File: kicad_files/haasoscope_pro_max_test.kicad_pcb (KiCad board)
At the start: 10 copper layers, 200 x 125 mm, 8 parts, among them IC1 ADC12DL500ACF_Aligned, U1 MT53D512M16D1DS_Aligned, U2 FT601Q_Aligned, U3 Ti90G529_Functions

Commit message: test_fanout_and_route.py from scratch
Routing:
- net Net-(U2A-DATA_11): track 8.84 -> 0.00 mm, vias 1 -> 0
- net Net-(U2A-DATA_14): track 8.73 -> 0.00 mm, vias 1 -> 0
- net Net-(U2A-DATA_17): track 8.20 -> 0.00 mm, vias 1 -> 0
- net Net-(U2A-DATA_20): track 8.20 -> 0.00 mm, vias 1 -> 0
- net Net-(U2A-DATA_0): track 7.93 -> 0.00 mm, vias 1 -> 0
- net Net-(U2A-DATA_16): track 6.87 -> 0.00 mm, vias 1 -> 0
- net Net-(U2A-DATA_2): track 6.70 -> 0.00 mm
- net Net-(U2A-DATA_23): track 6.60 -> 0.00 mm, vias 1 -> 0
- net Net-(U2A-DATA_22): track 6.07 -> 0.00 mm, vias 1 -> 0
- net Net-(U2A-DATA_5): track 5.90 -> 0.00 mm, vias 1 -> 0
- net Net-(U2A-DATA_9): track 5.80 -> 0.00 mm, vias 1 -> 0
- net Net-(U2A-DATA_24): track 5.64 -> 0.00 mm, vias 1 -> 0
- net Net-(U2A-DATA_8): track 5.53 -> 0.00 mm, vias 1 -> 0
- net Net-(U2A-DATA_18): track 5.53 -> 0.00 mm, vias 1 -> 0
- net Net-(U2A-DATA_13): track 5.37 -> 0.00 mm, vias 1 -> 0
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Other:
- board size 200 x 125 mm -> 110.6 x 48.6 mm

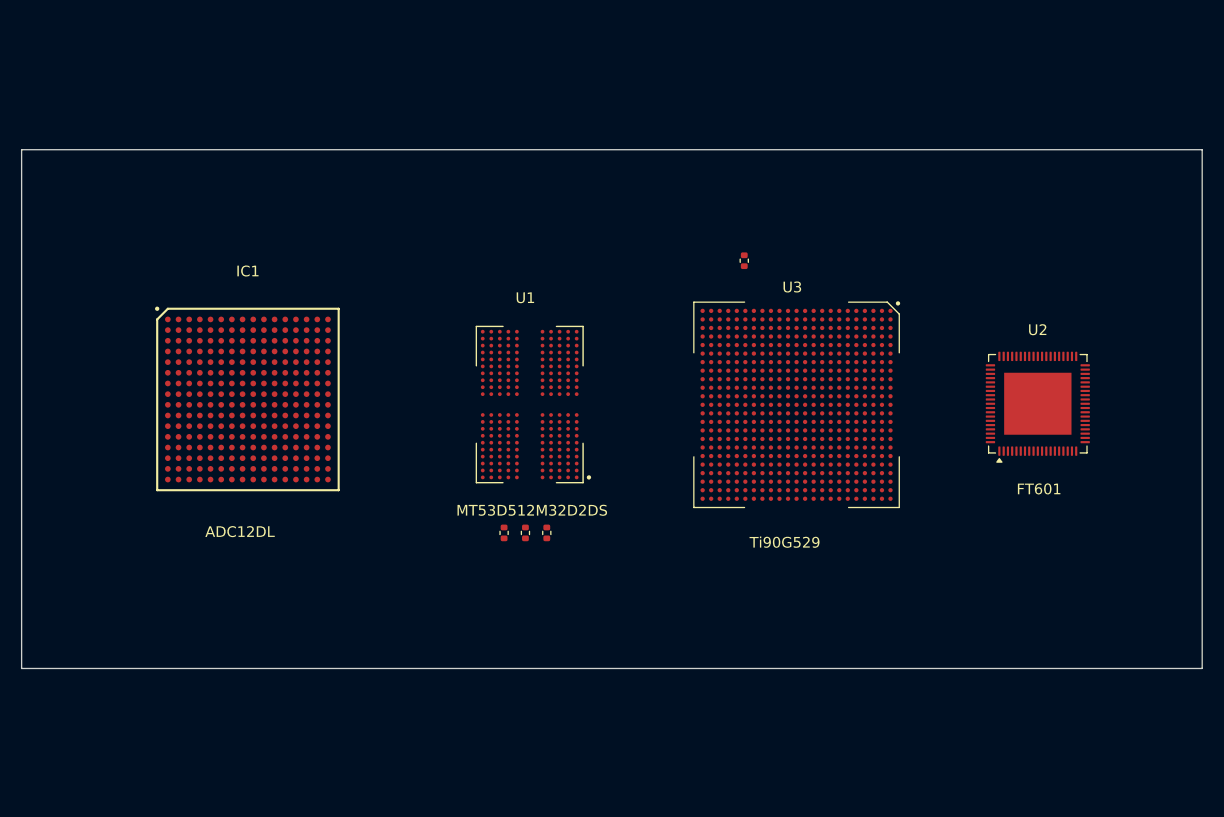
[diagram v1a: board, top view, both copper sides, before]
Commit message: --no-inner-top-layer for bga fanout
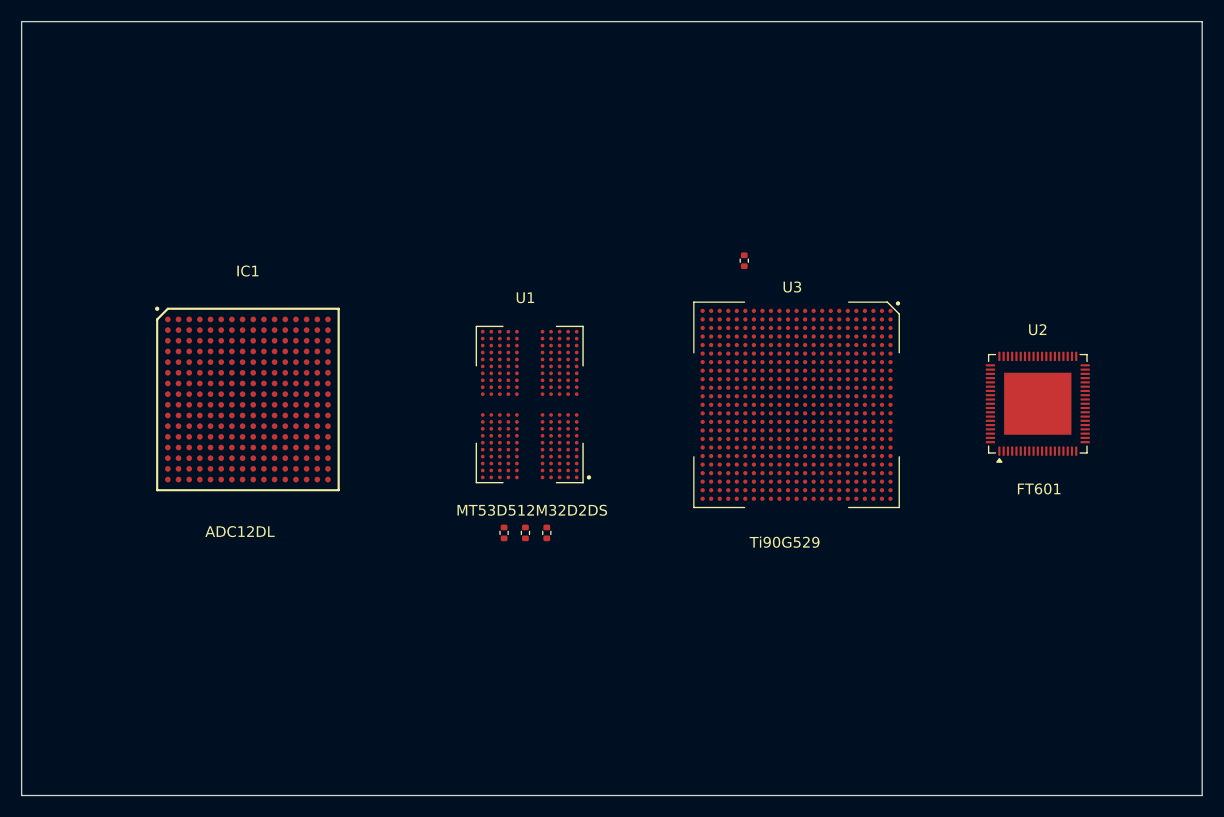
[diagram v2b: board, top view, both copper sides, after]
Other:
- board size 110.6 x 48.6 mm -> 110.6 x 72.5 mm
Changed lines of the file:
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@@
 	)
 	(gr_rect
-		(start 122.8 79.1)
-		(end 233.4 127.7)
+		(start 122.8 67.1)
+		(end 233.4 139.6)
 		(stroke
 			(width 0.05)

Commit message: add gnd plane
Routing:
- added copper zone on F.Cu, net GND
- added copper zone on In5.Cu, net GND
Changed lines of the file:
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@@
+		)
+	)
+	(zone
+		(net 690)
+		(net_name "GND")
+		(layers "F.Cu" "In5.Cu")
+		(hatch edge 0.5)
+		(connect_pads
+			(clearance 0.1)
+		)
+		(min_thickness 0.1)
+		(filled_areas_thickness no)
+		(fill yes
+			(thermal_gap 0.2)
+			(thermal_bridge_width 0.2)
+		)
+		(polygon
+			(pts
+				(xy 123.3 67.5) (xy 123.4 139) (xy 233 139.1) (xy 233.1 67.5)
+			)
 		)
 	)

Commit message: add gnd plane
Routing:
- removed copper zone on F.Cu, net GND
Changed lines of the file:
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@@
 		(net 690)
 		(net_name "GND")
-		(layers "F.Cu" "In5.Cu")
+		(layer "In5.Cu")
 		(hatch edge 0.5)
 		(connect_pads

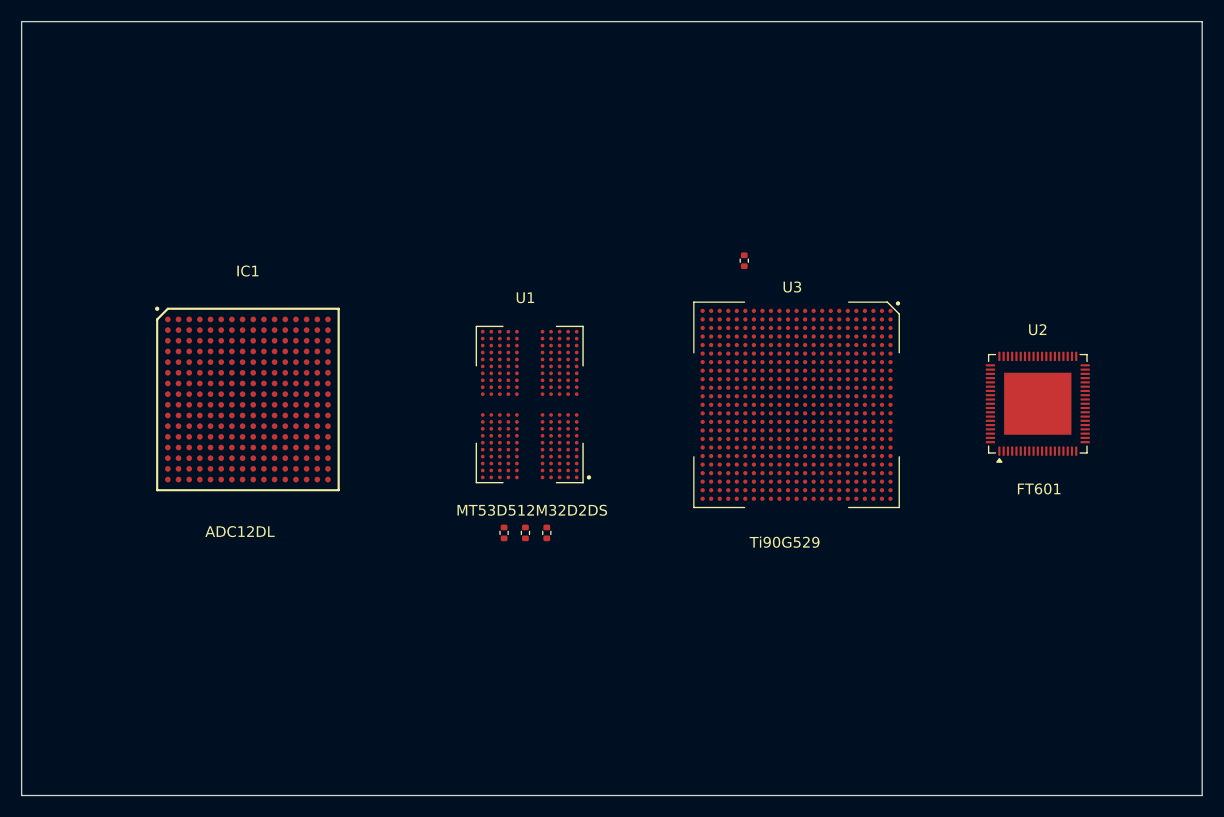
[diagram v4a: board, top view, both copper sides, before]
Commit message: HSPro max gnd and power test
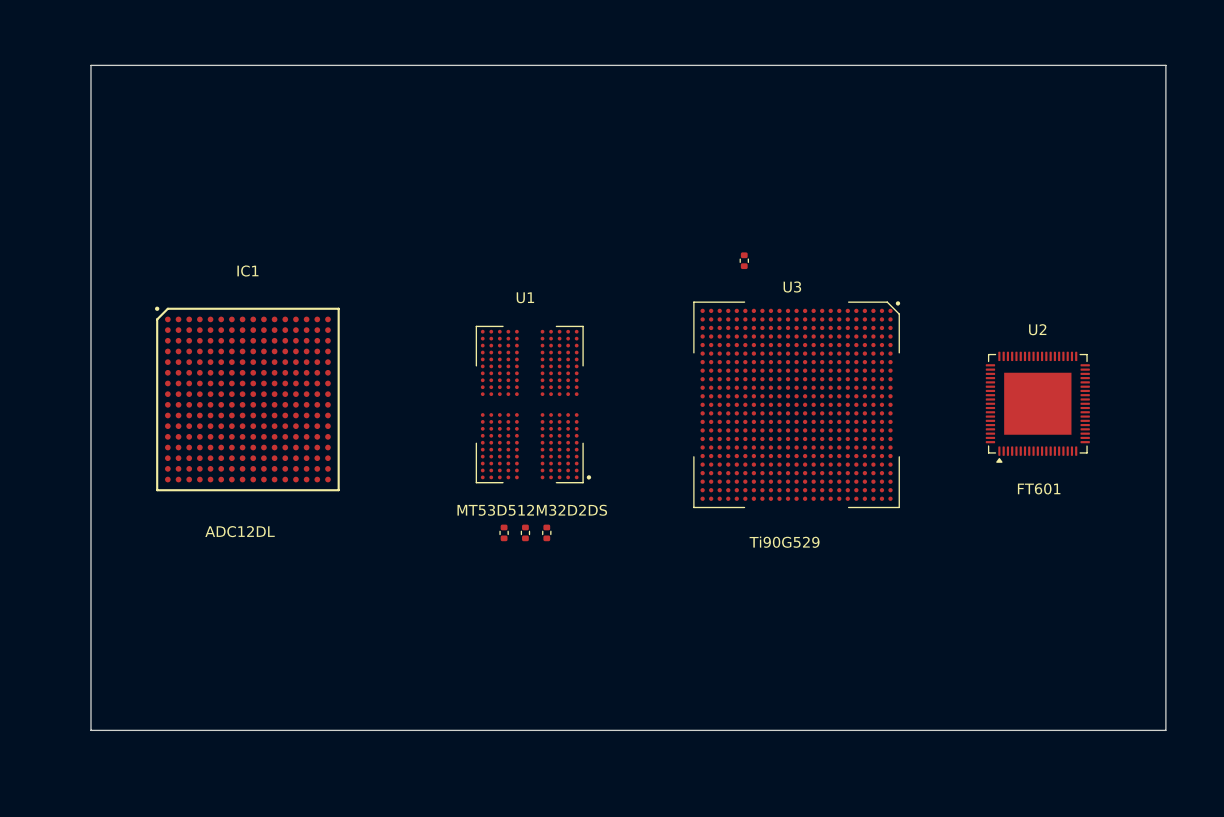
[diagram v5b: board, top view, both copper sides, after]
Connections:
- IC1 pad A1: unconnected-(IC1F-AGND_1-PadA1) -> GND
- IC1 pad A15: unconnected-(IC1F-DGND_1-PadA15) -> GND
- IC1 pad A16: unconnected-(IC1F-DGND_2-PadA16) -> GND
- IC1 pad A2: unconnected-(IC1F-AGND_2-PadA2) -> GND
- IC1 pad A3: unconnected-(IC1F-AGND_3-PadA3) -> GND
- IC1 pad A6: unconnected-(IC1F-AGND_4-PadA6) -> GND
- IC1 pad A7: unconnected-(IC1F-AGND_5-PadA7) -> GND
- IC1 pad B3: unconnected-(IC1F-AGND_6-PadB3) -> GND
- IC1 pad B4: unconnected-(IC1F-AGND_7-PadB4) -> GND
- IC1 pad B5: unconnected-(IC1F-AGND_8-PadB5) -> GND
- IC1 pad B6: unconnected-(IC1F-AGND_9-PadB6) -> GND
- IC1 pad B7: unconnected-(IC1F-AGND_10-PadB7) -> GND
- IC1 pad C1: unconnected-(IC1F-AGND_11-PadC1) -> GND
- IC1 pad C2: unconnected-(IC1F-AGND_12-PadC2) -> GND
- IC1 pad C3: unconnected-(IC1F-AGND_13-PadC3) -> GND
- IC1 pad C4: unconnected-(IC1F-AGND_14-PadC4) -> GND
- IC1 pad C5: unconnected-(IC1F-AGND_15-PadC5) -> GND
- IC1 pad C6: unconnected-(IC1F-AGND_16-PadC6) -> GND
- IC1 pad C7: unconnected-(IC1F-AGND_17-PadC7) -> GND
- IC1 pad D3: unconnected-(IC1F-AGND_18-PadD3) -> GND
- IC1 pad D4: unconnected-(IC1F-AGND_19-PadD4) -> GND
- IC1 pad D5: unconnected-(IC1F-AGND_20-PadD5) -> GND
- IC1 pad D6: unconnected-(IC1F-AGND_21-PadD6) -> GND
- IC1 pad D7: unconnected-(IC1F-DGND_3-PadD7) -> GND
- IC1 pad E3: unconnected-(IC1F-AGND_22-PadE3) -> GND
- IC1 pad E4: unconnected-(IC1F-VA11_1-PadE4) -> /fpga_adc/VA11
- IC1 pad E5: unconnected-(IC1F-VA11_2-PadE5) -> /fpga_adc/VA11
- IC1 pad E6: unconnected-(IC1F-VA11_3-PadE6) -> /fpga_adc/VA11
- IC1 pad E7: unconnected-(IC1F-DGND_4-PadE7) -> GND
- IC1 pad E8: unconnected-(IC1F-VD11_1-PadE8) -> /fpga_adc/VD11
- IC1 pad F1: unconnected-(IC1F-AGND_23-PadF1) -> GND
- IC1 pad F2: unconnected-(IC1F-AGND_24-PadF2) -> GND
- IC1 pad F3: unconnected-(IC1F-VA11_4-PadF3) -> /fpga_adc/VA11
- IC1 pad F4: unconnected-(IC1F-VA11_5-PadF4) -> /fpga_adc/VA11
- IC1 pad F5: unconnected-(IC1F-VA11_6-PadF5) -> /fpga_adc/VA11
- IC1 pad F6: unconnected-(IC1F-VA11_7-PadF6) -> /fpga_adc/VA11
- IC1 pad F7: unconnected-(IC1F-DGND_5-PadF7) -> GND
- IC1 pad F8: unconnected-(IC1F-VD11_2-PadF8) -> /fpga_adc/VD11
- IC1 pad G1: unconnected-(IC1F-AGND_25-PadG1) -> GND
- IC1 pad G11: unconnected-(IC1F-VLVDS_1-PadG11) -> /fpga_adc/VLVDS
- IC1 pad G12: unconnected-(IC1F-VLVDS_2-PadG12) -> /fpga_adc/VLVDS
- IC1 pad G2: unconnected-(IC1F-AGND_26-PadG2) -> GND
- IC1 pad G3: unconnected-(IC1F-VA19_1-PadG3) -> /fpga_adc/VA19
- IC1 pad G4: unconnected-(IC1F-VA19_2-PadG4) -> /fpga_adc/VA19
- IC1 pad G5: unconnected-(IC1F-VA19_3-PadG5) -> /fpga_adc/VA19
- IC1 pad G6: unconnected-(IC1F-VA19_4-PadG6) -> /fpga_adc/VA19
- IC1 pad G7: unconnected-(IC1F-DGND_6-PadG7) -> GND
- IC1 pad G8: unconnected-(IC1F-VD11_3-PadG8) -> /fpga_adc/VD11
- IC1 pad H11: unconnected-(IC1F-VLVDS_3-PadH11) -> /fpga_adc/VLVDS
- IC1 pad H12: unconnected-(IC1F-VLVDS_4-PadH12) -> /fpga_adc/VLVDS
- IC1 pad H13: unconnected-(IC1F-VLVDS_5-PadH13) -> /fpga_adc/VLVDS
- IC1 pad H14: unconnected-(IC1F-DGND_9-PadH14) -> GND
- IC1 pad H2: unconnected-(IC1F-AGND_27-PadH2) -> GND
- IC1 pad H3: unconnected-(IC1F-VA19_5-PadH3) -> /fpga_adc/VA19
- IC1 pad H4: unconnected-(IC1F-VA19_6-PadH4) -> /fpga_adc/VA19
- IC1 pad H5: unconnected-(IC1F-VA19_7-PadH5) -> /fpga_adc/VA19
- IC1 pad H6: unconnected-(IC1F-VA19_8-PadH6) -> /fpga_adc/VA19
- IC1 pad H7: unconnected-(IC1F-DGND_7-PadH7) -> GND
- IC1 pad H8: unconnected-(IC1F-DGND_8-PadH8) -> GND
- IC1 pad J11: unconnected-(IC1F-VLVDS_6-PadJ11) -> /fpga_adc/VLVDS
- IC1 pad J12: unconnected-(IC1F-VLVDS_7-PadJ12) -> /fpga_adc/VLVDS
- IC1 pad J13: unconnected-(IC1F-VLVDS_8-PadJ13) -> /fpga_adc/VLVDS
- IC1 pad J14: unconnected-(IC1F-DGND_12-PadJ14) -> GND
- IC1 pad J2: unconnected-(IC1F-AGND_28-PadJ2) -> GND
- IC1 pad J3: unconnected-(IC1F-VA19_9-PadJ3) -> /fpga_adc/VA19
- IC1 pad J4: unconnected-(IC1F-VA19_10-PadJ4) -> /fpga_adc/VA19
- IC1 pad J5: unconnected-(IC1F-VA19_11-PadJ5) -> /fpga_adc/VA19
- IC1 pad J6: unconnected-(IC1F-VA19_12-PadJ6) -> /fpga_adc/VA19
- IC1 pad J7: unconnected-(IC1F-DGND_10-PadJ7) -> GND
- IC1 pad J8: unconnected-(IC1F-DGND_11-PadJ8) -> GND
- IC1 pad K1: unconnected-(IC1F-AGND_29-PadK1) -> GND
- IC1 pad K11: unconnected-(IC1F-VLVDS_9-PadK11) -> /fpga_adc/VLVDS
- IC1 pad K12: unconnected-(IC1F-VLVDS_10-PadK12) -> /fpga_adc/VLVDS
- IC1 pad K2: unconnected-(IC1F-AGND_30-PadK2) -> GND
- IC1 pad K3: unconnected-(IC1F-VA19_13-PadK3) -> /fpga_adc/VA19
- IC1 pad K4: unconnected-(IC1F-VA19_14-PadK4) -> /fpga_adc/VA19
- IC1 pad K5: unconnected-(IC1F-VA19_15-PadK5) -> /fpga_adc/VA19
- IC1 pad K6: unconnected-(IC1F-VA19_16-PadK6) -> /fpga_adc/VA19
- IC1 pad K7: unconnected-(IC1F-DGND_13-PadK7) -> GND
- IC1 pad K8: unconnected-(IC1F-VD11_4-PadK8) -> /fpga_adc/VD11
- IC1 pad L1: unconnected-(IC1F-AGND_31-PadL1) -> GND
- IC1 pad L2: unconnected-(IC1F-AGND_32-PadL2) -> GND
- IC1 pad L3: unconnected-(IC1F-VA11_8-PadL3) -> /fpga_adc/VA11
- IC1 pad L4: unconnected-(IC1F-VA11_9-PadL4) -> /fpga_adc/VA11
- IC1 pad L5: unconnected-(IC1F-VA11_10-PadL5) -> /fpga_adc/VA11
- IC1 pad L6: unconnected-(IC1F-VA11_11-PadL6) -> /fpga_adc/VA11
- IC1 pad L7: unconnected-(IC1F-DGND_14-PadL7) -> GND
- IC1 pad L8: unconnected-(IC1F-VD11_5-PadL8) -> /fpga_adc/VD11
- IC1 pad M3: unconnected-(IC1F-AGND_33-PadM3) -> GND
- IC1 pad M4: unconnected-(IC1F-VA11_12-PadM4) -> /fpga_adc/VA11
- IC1 pad M5: unconnected-(IC1F-VA11_13-PadM5) -> /fpga_adc/VA11
- IC1 pad M6: unconnected-(IC1F-VA11_14-PadM6) -> /fpga_adc/VA11
- IC1 pad M7: unconnected-(IC1F-DGND_15-PadM7) -> GND
- IC1 pad M8: unconnected-(IC1F-VD11_6-PadM8) -> /fpga_adc/VD11
- IC1 pad N3: unconnected-(IC1F-AGND_34-PadN3) -> GND
- IC1 pad N4: unconnected-(IC1F-AGND_35-PadN4) -> GND
- IC1 pad N5: unconnected-(IC1F-AGND_36-PadN5) -> GND
- IC1 pad N6: unconnected-(IC1F-AGND_37-PadN6) -> GND
- IC1 pad N7: unconnected-(IC1F-DGND_16-PadN7) -> GND
- IC1 pad P1: unconnected-(IC1F-AGND_38-PadP1) -> GND
- IC1 pad P2: unconnected-(IC1F-AGND_39-PadP2) -> GND
- IC1 pad P3: unconnected-(IC1F-AGND_40-PadP3) -> GND
- IC1 pad P4: unconnected-(IC1F-AGND_41-PadP4) -> GND
- IC1 pad P5: unconnected-(IC1F-AGND_42-PadP5) -> GND
- IC1 pad P6: unconnected-(IC1F-AGND_43-PadP6) -> GND
- IC1 pad P7: unconnected-(IC1F-AGND_44-PadP7) -> GND
- IC1 pad R2: unconnected-(IC1F-AGND_45-PadR2) -> GND
- IC1 pad R3: unconnected-(IC1F-AGND_46-PadR3) -> GND
- IC1 pad R4: unconnected-(IC1F-AGND_47-PadR4) -> GND
- IC1 pad R5: unconnected-(IC1F-AGND_48-PadR5) -> GND
- IC1 pad R6: unconnected-(IC1F-AGND_49-PadR6) -> GND
- IC1 pad R7: unconnected-(IC1F-AGND_50-PadR7) -> GND
- IC1 pad T1: unconnected-(IC1F-AGND_51-PadT1) -> GND
- IC1 pad T15: unconnected-(IC1F-DGND_17-PadT15) -> GND
- IC1 pad T16: unconnected-(IC1F-DGND_18-PadT16) -> GND
- IC1 pad T2: unconnected-(IC1F-AGND_52-PadT2) -> GND
- IC1 pad T3: unconnected-(IC1F-AGND_53-PadT3) -> GND
- IC1 pad T6: unconnected-(IC1F-AGND_54-PadT6) -> GND
- IC1 pad T7: unconnected-(IC1F-AGND_55-PadT7) -> GND
- U1 pad A10: unconnected-(U1D-VSS-PadA10) -> GND
- U1 pad A3: unconnected-(U1D-VSS-PadA3) -> GND
- U1 pad A4: unconnected-(U1C-VDD2-PadA4) -> /fpga_ddr/VDD2
- U1 pad A9: unconnected-(U1C-VDD2-PadA9) -> /fpga_ddr/VDD2
- U1 pad AA10: unconnected-(U1C-VDDQ-PadAA10) -> /fpga_ddr/VDDQ
- U1 pad AA3: unconnected-(U1C-VDDQ-PadAA3) -> /fpga_ddr/VDDQ
- U1 pad AA5: unconnected-(U1C-VDDQ-PadAA5) -> /fpga_ddr/VDDQ
- U1 pad AA8: unconnected-(U1C-VDDQ-PadAA8) -> /fpga_ddr/VDDQ
- U1 pad AB10: unconnected-(U1D-VSS-PadAB10) -> GND
- U1 pad AB3: unconnected-(U1D-VSS-PadAB3) -> GND
- U1 pad AB4: unconnected-(U1C-VDD2-PadAB4) -> /fpga_ddr/VDD2
- U1 pad AB5: unconnected-(U1D-VSS-PadAB5) -> GND
- U1 pad AB8: unconnected-(U1D-VSS-PadAB8) -> GND
- U1 pad AB9: unconnected-(U1C-VDD2-PadAB9) -> /fpga_ddr/VDD2
- U1 pad B10: unconnected-(U1C-VDDQ-PadB10) -> /fpga_ddr/VDDQ
- U1 pad B3: unconnected-(U1C-VDDQ-PadB3) -> /fpga_ddr/VDDQ
- U1 pad B5: unconnected-(U1C-VDDQ-PadB5) -> /fpga_ddr/VDDQ
- U1 pad B8: unconnected-(U1C-VDDQ-PadB8) -> /fpga_ddr/VDDQ
- U1 pad C1: unconnected-(U1D-VSS-PadC1) -> GND
- U1 pad C12: unconnected-(U1D-VSS-PadC12) -> GND
- U1 pad C5: unconnected-(U1D-VSS-PadC5) -> GND
- U1 pad C8: unconnected-(U1D-VSS-PadC8) -> GND
- U1 pad D1: unconnected-(U1C-VDDQ-PadD1) -> /fpga_ddr/VDDQ
- U1 pad D11: unconnected-(U1D-VSS-PadD11) -> GND
- U1 pad D12: unconnected-(U1C-VDDQ-PadD12) -> /fpga_ddr/VDDQ
- U1 pad D2: unconnected-(U1D-VSS-PadD2) -> GND
- U1 pad D4: unconnected-(U1D-VSS-PadD4) -> GND
- U1 pad D5: unconnected-(U1C-VDDQ-PadD5) -> /fpga_ddr/VDDQ
- U1 pad D8: unconnected-(U1C-VDDQ-PadD8) -> /fpga_ddr/VDDQ
- U1 pad D9: unconnected-(U1D-VSS-PadD9) -> GND
- U1 pad E1: unconnected-(U1D-VSS-PadE1) -> GND
- U1 pad E12: unconnected-(U1D-VSS-PadE12) -> GND
- U1 pad E5: unconnected-(U1D-VSS-PadE5) -> GND
- U1 pad E8: unconnected-(U1D-VSS-PadE8) -> GND
- U1 pad F1: unconnected-(U1C-VDD1-PadF1) -> /fpga_ddr/VDD1
- U1 pad F10: unconnected-(U1C-VDDQ-PadF10) -> /fpga_ddr/VDDQ
- U1 pad F12: unconnected-(U1C-VDD1-PadF12) -> /fpga_ddr/VDD1
- U1 pad F3: unconnected-(U1C-VDDQ-PadF3) -> /fpga_ddr/VDDQ
- U1 pad F5: unconnected-(U1C-VDD2-PadF5) -> /fpga_ddr/VDD2
- U1 pad F8: unconnected-(U1C-VDD2-PadF8) -> /fpga_ddr/VDD2
- U1 pad G1: unconnected-(U1D-VSS-PadG1) -> GND
- U1 pad G10: unconnected-(U1D-VSS-PadG10) -> GND
- U1 pad G12: unconnected-(U1D-VSS-PadG12) -> GND
- U1 pad G3: unconnected-(U1D-VSS-PadG3) -> GND
- U1 pad G4: unconnected-(U1C-VDD1-PadG4) -> /fpga_ddr/VDD1
- U1 pad G5: unconnected-(U1D-VSS-PadG5) -> GND
- U1 pad G8: unconnected-(U1D-VSS-PadG8) -> GND
- U1 pad G9: unconnected-(U1C-VDD1-PadG9) -> /fpga_ddr/VDD1
- U1 pad H1: unconnected-(U1C-VDD2-PadH1) -> /fpga_ddr/VDD2
- U1 pad H12: unconnected-(U1C-VDD2-PadH12) -> /fpga_ddr/VDD2
- U1 pad H5: unconnected-(U1C-VDD2-PadH5) -> /fpga_ddr/VDD2
- U1 pad H8: unconnected-(U1C-VDD2-PadH8) -> /fpga_ddr/VDD2
- U1 pad J1: unconnected-(U1D-VSS-PadJ1) -> GND
- U1 pad J10: unconnected-(U1D-VSS-PadJ10) -> GND
- U1 pad J12: unconnected-(U1D-VSS-PadJ12) -> GND
- U1 pad J3: unconnected-(U1D-VSS-PadJ3) -> GND
- U1 pad K1: unconnected-(U1C-VDD2-PadK1) -> /fpga_ddr/VDD2
- U1 pad K10: unconnected-(U1C-VDD2-PadK10) -> /fpga_ddr/VDD2
- U1 pad K11: unconnected-(U1D-VSS-PadK11) -> GND
- U1 pad K12: unconnected-(U1C-VDD2-PadK12) -> /fpga_ddr/VDD2
- U1 pad K2: unconnected-(U1D-VSS-PadK2) -> GND
- U1 pad K3: unconnected-(U1C-VDD2-PadK3) -> /fpga_ddr/VDD2
- U1 pad K4: unconnected-(U1D-VSS-PadK4) -> GND
- U1 pad K9: unconnected-(U1D-VSS-PadK9) -> GND
- U1 pad N1: unconnected-(U1C-VDD2-PadN1) -> /fpga_ddr/VDD2
- U1 pad N10: unconnected-(U1C-VDD2-PadN10) -> /fpga_ddr/VDD2
- U1 pad N11: unconnected-(U1D-VSS-PadN11) -> GND
- U1 pad N12: unconnected-(U1C-VDD2-PadN12) -> /fpga_ddr/VDD2
- U1 pad N2: unconnected-(U1D-VSS-PadN2) -> GND
- U1 pad N3: unconnected-(U1C-VDD2-PadN3) -> /fpga_ddr/VDD2
- U1 pad N4: unconnected-(U1D-VSS-PadN4) -> GND
- U1 pad N9: unconnected-(U1D-VSS-PadN9) -> GND
- U1 pad P1: unconnected-(U1D-VSS-PadP1) -> GND
- U1 pad P10: unconnected-(U1D-VSS-PadP10) -> GND
- U1 pad P12: unconnected-(U1D-VSS-PadP12) -> GND
- U1 pad P3: unconnected-(U1D-VSS-PadP3) -> GND
- U1 pad R1: unconnected-(U1C-VDD2-PadR1) -> /fpga_ddr/VDD2
- U1 pad R12: unconnected-(U1C-VDD2-PadR12) -> /fpga_ddr/VDD2
- U1 pad R5: unconnected-(U1C-VDD2-PadR5) -> /fpga_ddr/VDD2
- U1 pad R8: unconnected-(U1C-VDD2-PadR8) -> /fpga_ddr/VDD2
- U1 pad T1: unconnected-(U1D-VSS-PadT1) -> GND
- U1 pad T10: unconnected-(U1D-VSS-PadT10) -> GND
- U1 pad T12: unconnected-(U1D-VSS-PadT12) -> GND
- U1 pad T3: unconnected-(U1D-VSS-PadT3) -> GND
- U1 pad T4: unconnected-(U1C-VDD1-PadT4) -> /fpga_ddr/VDD1
- U1 pad T5: unconnected-(U1D-VSS-PadT5) -> GND
- U1 pad T8: unconnected-(U1D-VSS-PadT8) -> GND
- U1 pad T9: unconnected-(U1C-VDD1-PadT9) -> /fpga_ddr/VDD1
- U1 pad U1: unconnected-(U1C-VDD1-PadU1) -> /fpga_ddr/VDD1
- U1 pad U10: unconnected-(U1C-VDDQ-PadU10) -> /fpga_ddr/VDDQ
- U1 pad U12: unconnected-(U1C-VDD1-PadU12) -> /fpga_ddr/VDD1
- U1 pad U3: unconnected-(U1C-VDDQ-PadU3) -> /fpga_ddr/VDDQ
- U1 pad U5: unconnected-(U1C-VDD2-PadU5) -> /fpga_ddr/VDD2
- U1 pad U8: unconnected-(U1C-VDD2-PadU8) -> /fpga_ddr/VDD2
- U1 pad V1: unconnected-(U1D-VSS-PadV1) -> GND
- U1 pad V12: unconnected-(U1D-VSS-PadV12) -> GND
- U1 pad V5: unconnected-(U1D-VSS-PadV5) -> GND
- U1 pad V8: unconnected-(U1D-VSS-PadV8) -> GND
- U1 pad W1: unconnected-(U1C-VDDQ-PadW1) -> /fpga_ddr/VDDQ
- U1 pad W11: unconnected-(U1D-VSS-PadW11) -> GND
- U1 pad W12: unconnected-(U1C-VDDQ-PadW12) -> /fpga_ddr/VDDQ
- U1 pad W2: unconnected-(U1D-VSS-PadW2) -> GND
- U1 pad W4: unconnected-(U1D-VSS-PadW4) -> GND
- U1 pad W5: unconnected-(U1C-VDDQ-PadW5) -> /fpga_ddr/VDDQ
- U1 pad W8: unconnected-(U1C-VDDQ-PadW8) -> /fpga_ddr/VDDQ
- U1 pad W9: unconnected-(U1D-VSS-PadW9) -> GND
- U1 pad Y1: unconnected-(U1D-VSS-PadY1) -> GND
- U1 pad Y12: unconnected-(U1D-VSS-PadY12) -> GND
- U1 pad Y5: unconnected-(U1D-VSS-PadY5) -> GND
- U1 pad Y8: unconnected-(U1D-VSS-PadY8) -> GND
- U2 pad 1: unconnected-(U2C-GND-Pad1) -> GND
- U2 pad 19: unconnected-(U2C-GND-Pad19) -> GND
- U2 pad 26: unconnected-(U2C-GND-Pad26) -> GND
- U2 pad 29: unconnected-(U2C-GND-Pad29) -> GND
- U2 pad 36: unconnected-(U2C-GND-Pad36) -> GND
- U2 pad 77: unconnected-(U2C-GND-Pad77) -> GND
- U3 pad A1: unconnected-(U3I-GND-PadA1) -> GND
- U3 pad A19: unconnected-(U3I-GND-PadA19) -> GND
- U3 pad A23: unconnected-(U3I-GND-PadA23) -> GND
- U3 pad AA19: unconnected-(U3I-GND-PadAA19) -> GND
- U3 pad AB11: unconnected-(U3I-GND-PadAB11) -> GND
- U3 pad AB13: unconnected-(U3I-GND-PadAB13) -> GND
- U3 pad AB17: unconnected-(U3I-GND-PadAB17) -> GND
- U3 pad AB2: unconnected-(U3I-GND-PadAB2) -> GND
- U3 pad AB22: unconnected-(U3I-GND-PadAB22) -> GND
- U3 pad AB5: unconnected-(U3I-GND-PadAB5) -> GND
- U3 pad AB7: unconnected-(U3I-GND-PadAB7) -> GND
- U3 pad AC1: unconnected-(U3I-GND-PadAC1) -> GND
- U3 pad AC15: unconnected-(U3I-GND-PadAC15) -> GND
- U3 pad AC20: unconnected-(U3I-GND-PadAC20) -> GND
- U3 pad AC23: unconnected-(U3I-GND-PadAC23) -> GND
- U3 pad AC4: unconnected-(U3I-GND-PadAC4) -> GND
- U3 pad AC9: unconnected-(U3I-GND-PadAC9) -> GND
- U3 pad B11: unconnected-(U3I-GND-PadB11) -> GND
- U3 pad B14: unconnected-(U3I-GND-PadB14) -> GND
- U3 pad B21: unconnected-(U3I-GND-PadB21) -> GND
- U3 pad B3: unconnected-(U3I-GND-PadB3) -> GND
- U3 pad B6: unconnected-(U3I-GND-PadB6) -> GND
- U3 pad D1: unconnected-(U3I-GND-PadD1) -> GND
- U3 pad D10: unconnected-(U3I-GND-PadD10) -> GND
- U3 pad D19: unconnected-(U3I-GND-PadD19) -> GND
- U3 pad D22: unconnected-(U3I-GND-PadD22) -> GND
- U3 pad F2: unconnected-(U3I-GND-PadF2) -> GND
- U3 pad F20: unconnected-(U3I-GND-PadF20) -> GND
- U3 pad F22: unconnected-(U3I-GND-PadF22) -> GND
- U3 pad H1: unconnected-(U3I-GND-PadH1) -> GND
- U3 pad H23: unconnected-(U3I-GND-PadH23) -> GND
- U3 pad H4: unconnected-(U3I-GND-PadH4) -> GND
- U3 pad H7: unconnected-(U3I-GND-PadH7) -> GND
- U3 pad J10: unconnected-(U3I-GND-PadJ10) -> GND
- U3 pad J12: unconnected-(U3I-GND-PadJ12) -> GND
- U3 pad J14: unconnected-(U3I-GND-PadJ14) -> GND
- U3 pad J19: unconnected-(U3I-GND-PadJ19) -> GND
- U3 pad K11: unconnected-(U3I-GND-PadK11) -> GND
- U3 pad K13: unconnected-(U3I-GND-PadK13) -> GND
- U3 pad K15: unconnected-(U3I-GND-PadK15) -> GND
- U3 pad K2: unconnected-(U3I-GND-PadK2) -> GND
- U3 pad K5: unconnected-(U3I-GND-PadK5) -> GND
- U3 pad K9: unconnected-(U3I-GND-PadK9) -> GND
- U3 pad L10: unconnected-(U3I-GND-PadL10) -> GND
- U3 pad L12: unconnected-(U3I-GND-PadL12) -> GND
- U3 pad L14: unconnected-(U3I-GND-PadL14) -> GND
- U3 pad M1: unconnected-(U3I-GND-PadM1) -> GND
- U3 pad M11: unconnected-(U3I-GND-PadM11) -> GND
- U3 pad M13: unconnected-(U3I-GND-PadM13) -> GND
- U3 pad M15: unconnected-(U3I-GND-PadM15) -> GND
- U3 pad M20: unconnected-(U3I-GND-PadM20) -> GND
- U3 pad M23: unconnected-(U3I-GND-PadM23) -> GND
- U3 pad M3: unconnected-(U3I-GND-PadM3) -> GND
- U3 pad M9: unconnected-(U3I-GND-PadM9) -> GND
- U3 pad N10: unconnected-(U3I-GND-PadN10) -> GND
- U3 pad N12: unconnected-(U3I-GND-PadN12) -> GND
- U3 pad N14: unconnected-(U3I-GND-PadN14) -> GND
- U3 pad N8: unconnected-(U3I-GND-PadN8) -> GND
- U3 pad P10: unconnected-(U3I-GND-PadP10) -> GND
- U3 pad P13: unconnected-(U3I-GND-PadP13) -> GND
- U3 pad P16: unconnected-(U3I-GND-PadP16) -> GND
- U3 pad R12: unconnected-(U3I-GND-PadR12) -> GND
- U3 pad R15: unconnected-(U3I-GND-PadR15) -> GND
- U3 pad R9: unconnected-(U3I-GND-PadR9) -> GND
- U3 pad T1: unconnected-(U3I-GND-PadT1) -> GND
- U3 pad T17: unconnected-(U3I-GND-PadT17) -> GND
- U3 pad T21: unconnected-(U3I-GND-PadT21) -> GND
- U3 pad T23: unconnected-(U3I-GND-PadT23) -> GND
- U3 pad T7: unconnected-(U3I-GND-PadT7) -> GND
- U3 pad U11: unconnected-(U3I-GND-PadU11) -> GND
- U3 pad U14: unconnected-(U3I-GND-PadU14) -> GND
- U3 pad V10: unconnected-(U3I-GND-PadV10) -> GND
- U3 pad V13: unconnected-(U3I-GND-PadV13) -> GND
- U3 pad V15: unconnected-(U3I-GND-PadV15) -> GND
- U3 pad V17: unconnected-(U3I-GND-PadV17) -> GND
- U3 pad V7: unconnected-(U3I-GND-PadV7) -> GND
- U3 pad Y10: unconnected-(U3I-GND-PadY10) -> GND
- U3 pad Y12: unconnected-(U3I-GND-PadY12) -> GND
- U3 pad Y14: unconnected-(U3I-GND-PadY14) -> GND
- U3 pad Y16: unconnected-(U3I-GND-PadY16) -> GND
- U3 pad Y18: unconnected-(U3I-GND-PadY18) -> GND
- U3 pad Y2: unconnected-(U3I-GND-PadY2) -> GND
- U3 pad Y20: unconnected-(U3I-GND-PadY20) -> GND
- U3 pad Y22: unconnected-(U3I-GND-PadY22) -> GND
- U3 pad Y4: unconnected-(U3I-GND-PadY4) -> GND
- U3 pad Y6: unconnected-(U3I-GND-PadY6) -> GND
- U3 pad Y8: unconnected-(U3I-GND-PadY8) -> GND
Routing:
- removed copper zone on In5.Cu, net GND
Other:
- board size 110.6 x 72.5 mm -> 100.7 x 62.3 mm
